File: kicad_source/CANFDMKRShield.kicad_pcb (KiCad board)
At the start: 2 copper layers, 60 x 23 mm, 13 parts, among them CN1 ARDUINO_MKR, CN2 CONN_01X04, SW1 SWITCH_SMALL, U1 MCP2517FD, U2 SN65HVD232, Y1 20MHz

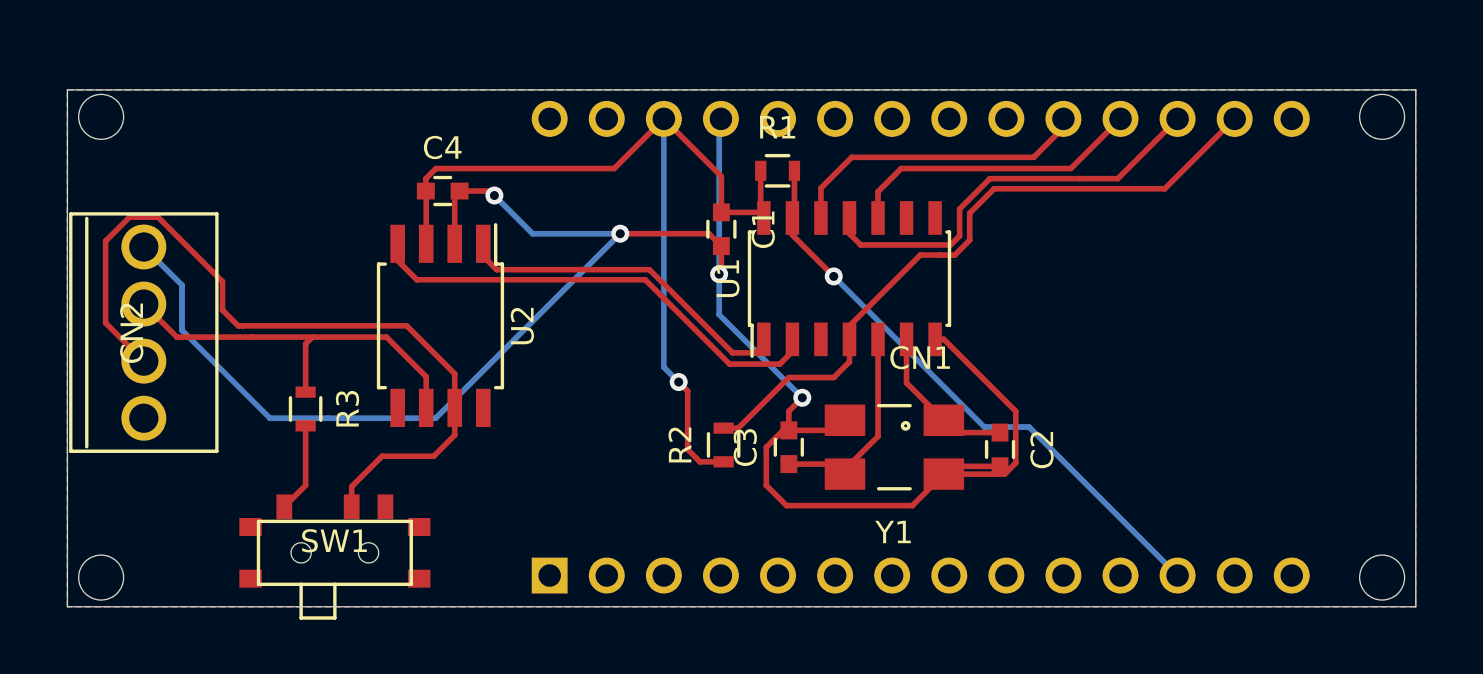
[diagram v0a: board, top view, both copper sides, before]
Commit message: added voltage regulators, updated images and pdf schematic
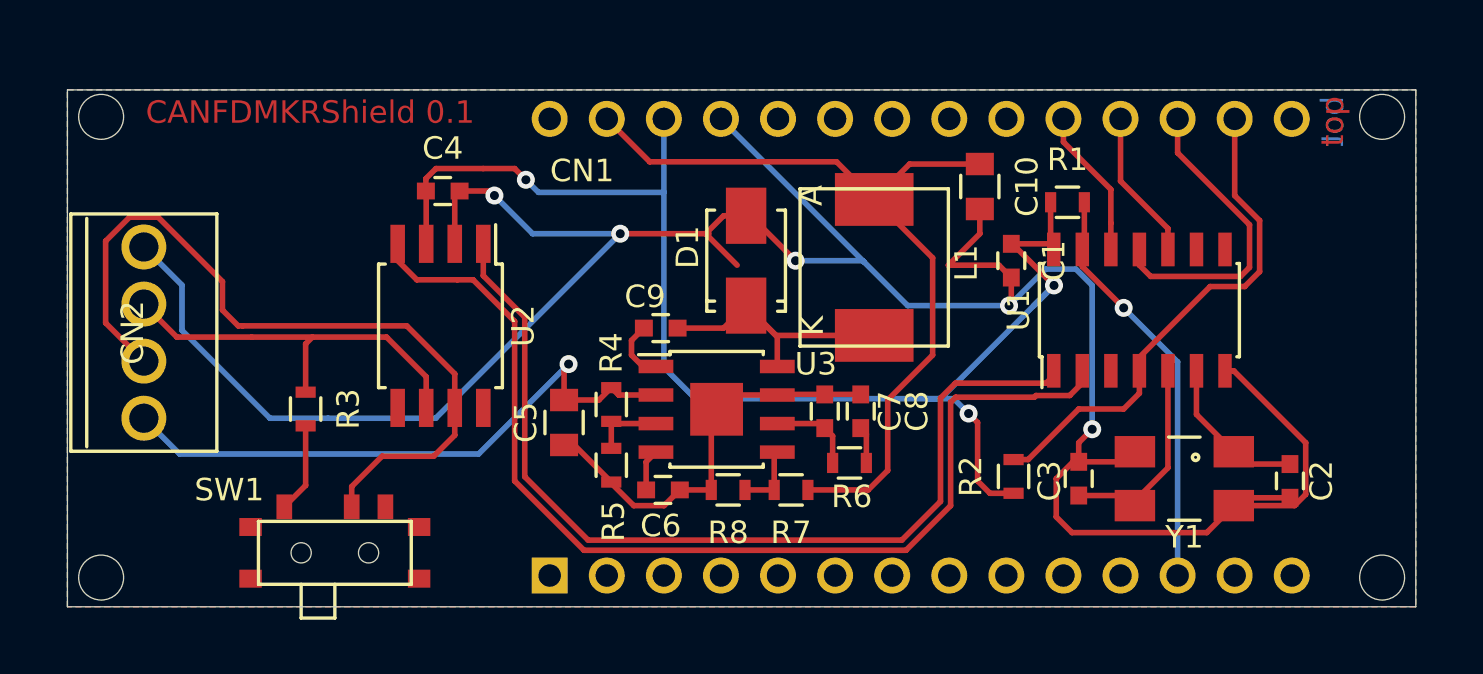
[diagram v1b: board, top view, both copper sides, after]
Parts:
- added C10: 10uF, capacitors:C_0805, F.Cu at (148.6, 93.3)
- added C5: 10uF, capacitors:C_0805, F.Cu at (130.1, 103.8)
- added C6: 4.7 nF, capacitors:C_0603, F.Cu at (134.5, 106.8)
- added C7: 110pF, capacitors:C_0603, F.Cu at (141.7, 103.3)
- added C8: 4.7 nF, capacitors:C_0603, F.Cu at (143.3, 103.3)
- added C9: 100nF, capacitors:C_0603, F.Cu at (134.4, 99.6)
- added D1: SSA34, diodes:SMA_Standard, F.Cu at (138.2, 96.6)
- added L1: 0624CDMCCDS-220MC, L_power:Sumida-0624CDMCCDS, F.Cu at (143.9, 96.9)
- added L2: Label, labels:generationmake_small_solder, F.Cu at (168.3, 100.2)
- added R4: DNI, resistors:R_0603, F.Cu at (132.2, 103.0)
- added R5: DNI, resistors:R_0603, F.Cu at (132.2, 105.7)
- added R6: 12k7, resistors:R_0603, F.Cu at (142.8, 105.6)
- added R7: 10k, resistors:R_0603, F.Cu at (140.2, 106.8)
- added R8: 1k9, resistors:R_0603, F.Cu at (137.4, 106.8)
- added U3: TPS54232, SOIC:SOIC-8-1EP_3.9x4.9mm_Pitch1.27mm, F.Cu at (136.9, 103.2)
- moved C1 13.0 mm to (150.0, 96.6)
- moved C2 13.0 mm to (162.4, 106.4)
- moved C3 13.0 mm to (153.0, 106.3)
- moved R1 13.0 mm to (152.5, 94.0)
- moved R2 13.0 mm to (150.1, 106.2)
- moved U1 13.0 mm to (155.7, 98.8)
- moved Y1 13.0 mm to (157.7, 106.3)
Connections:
- CN1 pad 27: (no net) -> +5V
- CN2 pad 4: (no net) -> VCC
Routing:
- net GND: track 88.8 -> 136.9 mm, vias 4 -> 5
- net +5V: track 0.00 -> 36.6 mm
- net VCC: track 0.00 -> 27.3 mm, vias 0 -> 1
- net /CAN_TX: track 15.2 -> 41.8 mm
- net /CAN_RX: track 21.0 -> 47.0 mm
- net +3V3: track 41.0 -> 60.5 mm, vias 1 -> 3
- net /PH: track 0.00 -> 13.0 mm
- net /MCP2517_CS: track 26.3 -> 18.4 mm
- net /MCP2517_INT: track 30.1 -> 22.6 mm
- net /MISO: track 13.6 -> 6.68 mm
- net /SCK: track 13.3 -> 6.68 mm
- net /MOSI: track 18.5 -> 13.9 mm
- net /COMP: track 0.00 -> 3.89 mm
- net /EN: track 0.00 -> 3.23 mm
- net /VSENSE: track 0.00 -> 3.04 mm
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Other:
- board text added: "CANFDMKRShield 0.1"
- board text added: "bot"
- board text added: "top"

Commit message: added dronecode CAN connectors, updated images and schematic pdf
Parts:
- added CN3: GH_SM04B-GHS-TB, Connector_JST:JST_GH_SM04B-GHS-TB_1x04-1MP_P1.25mm_Horizontal, F.Cu at (111.2, 96.0)
- added CN4: GH_SM04B-GHS-TB, Connector_JST:JST_GH_SM04B-GHS-TB_1x04-1MP_P1.25mm_Horizontal, F.Cu at (111.2, 104.9)
- moved CN2 11.7 mm to (120.4, 92.3), turned to 180 degrees
- moved R3 2.82 mm to (117.8, 105.9), turned to 180 degrees
- moved C4 2.77 mm to (126.8, 95.3), turned to 270 degrees
- moved U2 2.30 mm to (124.7, 101.8)
- moved L2 2.19 mm to (166.8, 98.6)
- moved SW1 0.61 mm to (119.3, 109.5)
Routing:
- net +5V: track 36.6 -> 79.2 mm, vias 0 -> 2
- net /CANL: track 17.9 -> 48.4 mm
- net GND: track 136.9 -> 152.5 mm, vias 5 -> 8
- net /CANH: track 34.8 -> 49.3 mm, vias 0 -> 2
- net VCC: track 27.3 -> 24.3 mm
- net Net-(R3-Pad2): track 3.99 -> 1.55 mm
- net /CAN_RX: track 47.0 -> 45.2 mm
- net +3V3: track 60.5 -> 59.8 mm

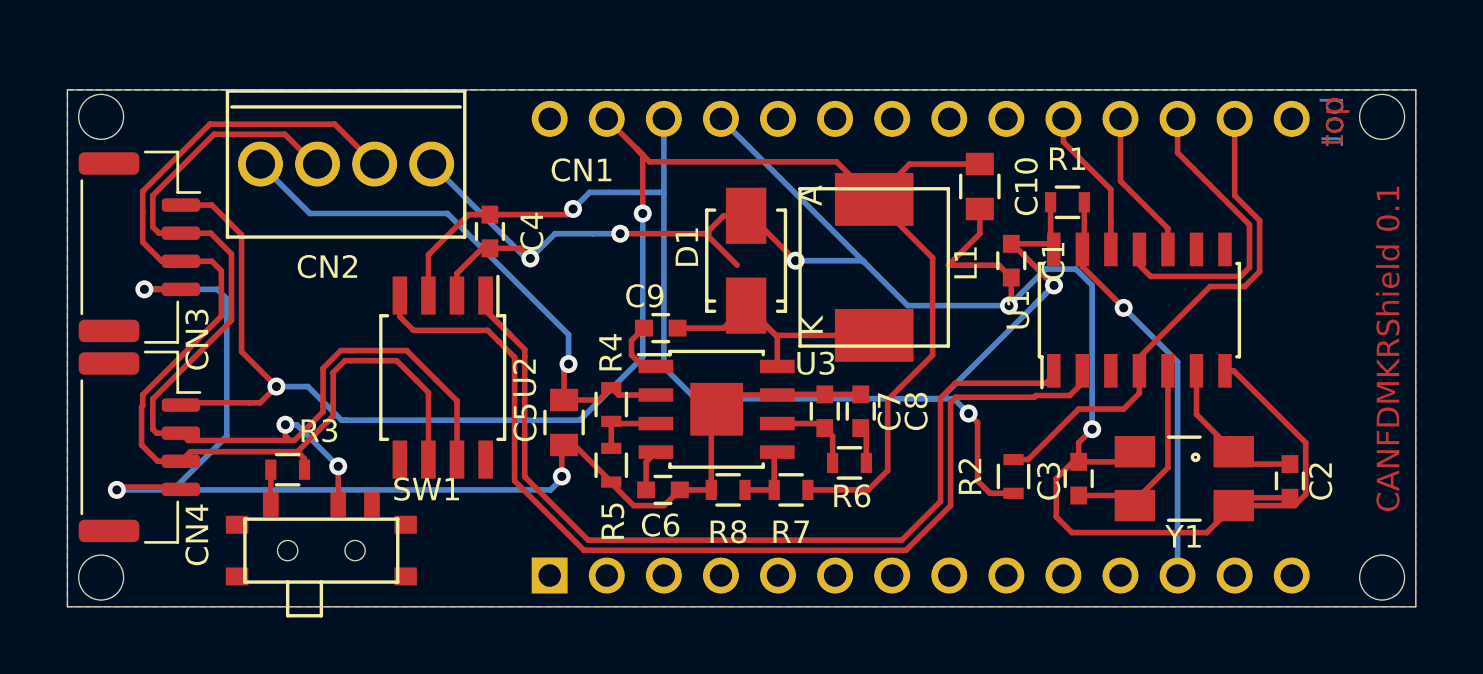
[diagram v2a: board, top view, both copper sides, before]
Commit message: updated board shape, changed switch type
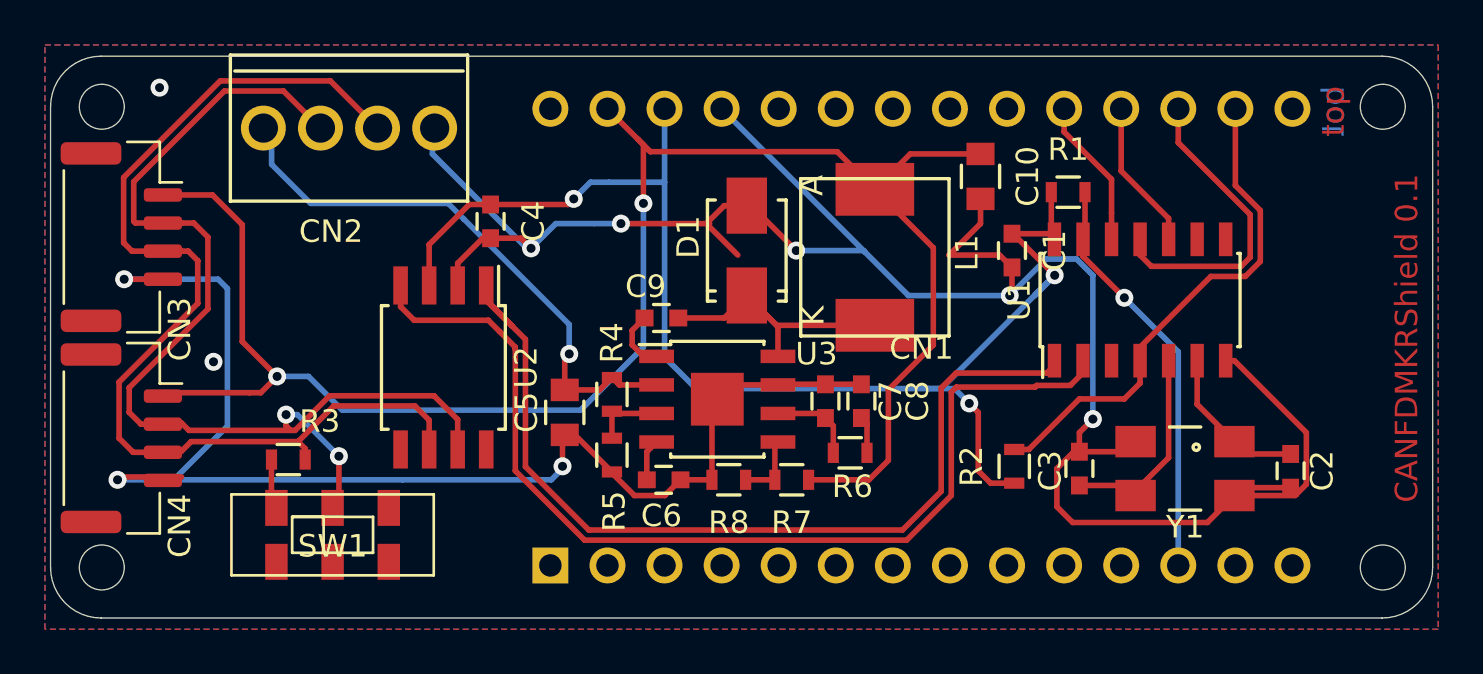
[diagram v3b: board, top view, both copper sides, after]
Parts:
- CN1: footprint MODULE_compute:ARDUINO_MKR_HOLES -> MODULE_compute:ARDUINO_MKR_HOLES_PINHEADER_EDGE
- SW1: value SWITCH_SMALL -> JS202011JCQN; footprint mechanical-switches:WE_450404015514 -> mechanical-switches:CK_JS202011JCQN
- moved CN2 1.61 mm to (120.5, 90.7)
- moved CN3 0.92 mm to (110.4, 95.5)
- moved CN4 0.89 mm to (110.4, 104.5)
- moved SW1 0.86 mm to (119.8, 108.8), turned to 0 degrees
- moved C10 0.45 mm to (148.6, 92.8)
- moved C2 0.45 mm to (162.4, 106.0)
- moved C3 0.45 mm to (153.0, 105.8)
- moved C4 0.45 mm to (126.8, 94.8)
- moved C5 0.45 mm to (130.1, 103.3)
- moved C6 0.45 mm to (134.5, 106.3)
- moved C7 0.45 mm to (141.7, 102.8)
- moved C8 0.45 mm to (143.3, 102.8)
- moved CN1 0.45 mm to (146.0, 100.0)
- moved L1 0.45 mm to (143.9, 96.5)
- moved R1 0.45 mm to (152.5, 93.5)
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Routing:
- net GND: track 152.5 -> 154.7 mm, vias 8 -> 10
- net VCC: track 24.3 -> 25.4 mm
- net /CANL: track 48.4 -> 47.4 mm
- net /CANH: track 49.3 -> 48.6 mm
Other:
- board size 60 x 23 mm -> 61.5 x 25 mm

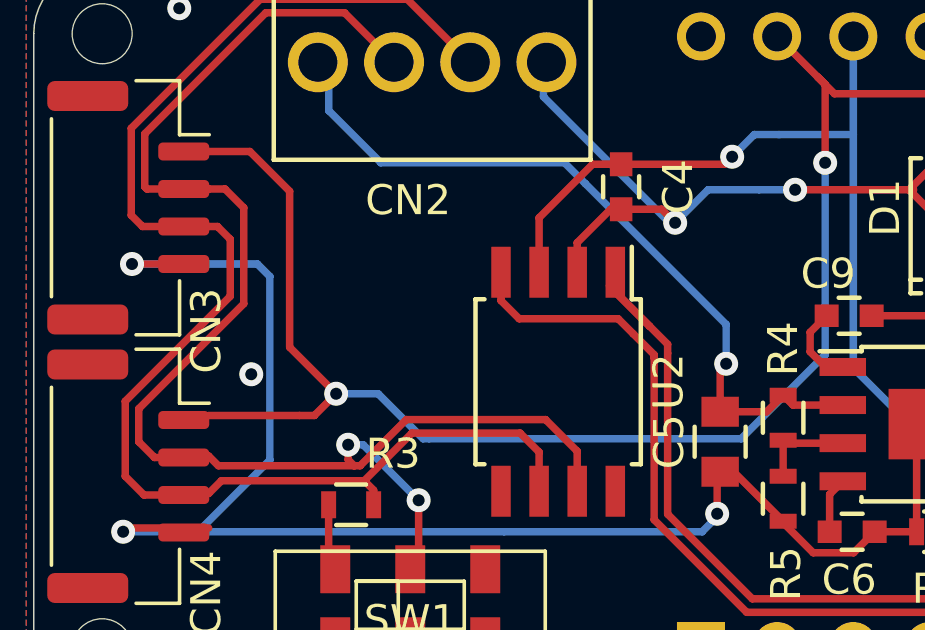
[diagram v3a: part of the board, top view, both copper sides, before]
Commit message: added diode D2 to connect CAN VCC to 5V
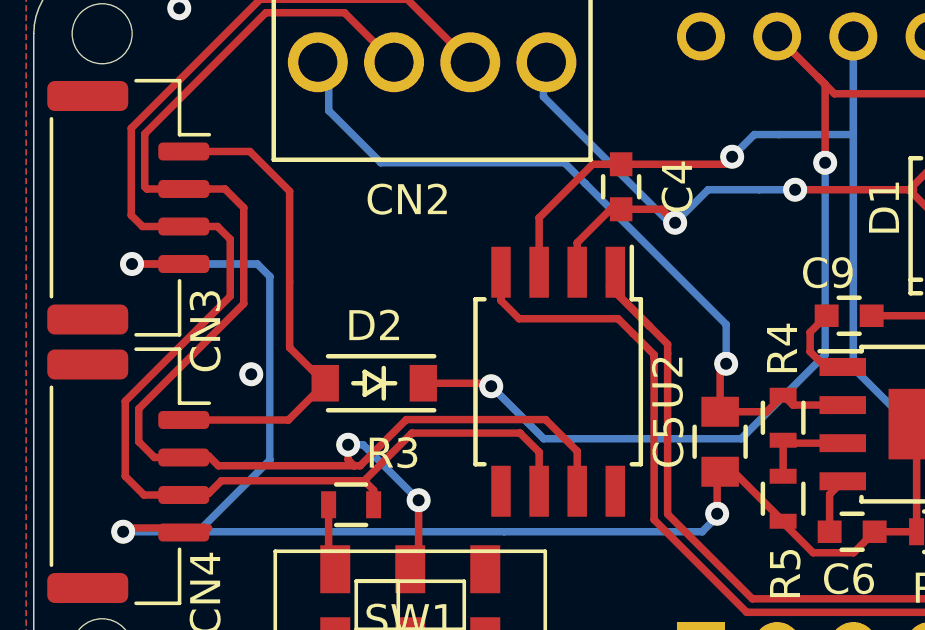
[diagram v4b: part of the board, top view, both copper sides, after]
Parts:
- added D2: DNI, diodes:SOD-123, F.Cu at (118.6, 101.4)
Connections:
- CN3 pad 1: +5V -> /CANVCC
- CN4 pad 1: +5V -> /CANVCC
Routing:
- net +5V: track 79.2 -> 61.3 mm
- net /CANVCC: track 0.00 -> 15.4 mm

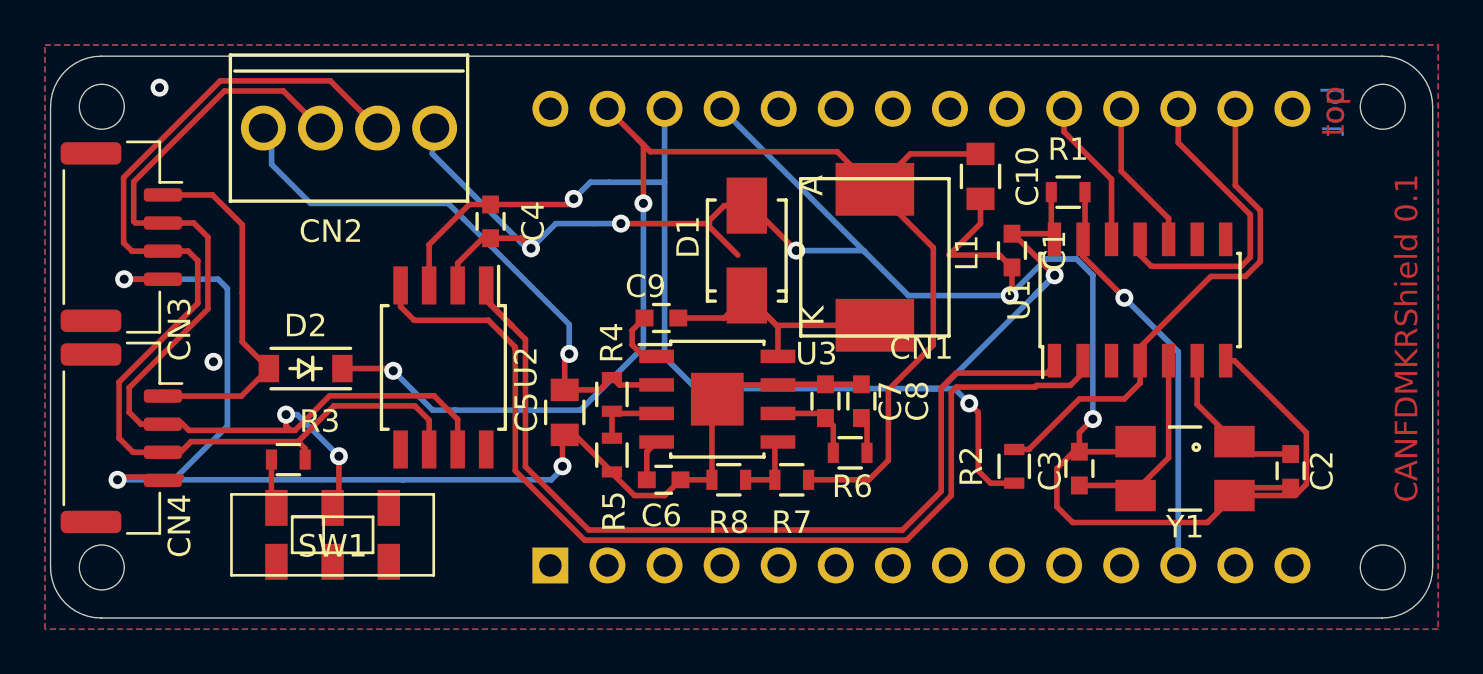
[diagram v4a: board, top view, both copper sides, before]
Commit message: added option to use different CS line for SPI
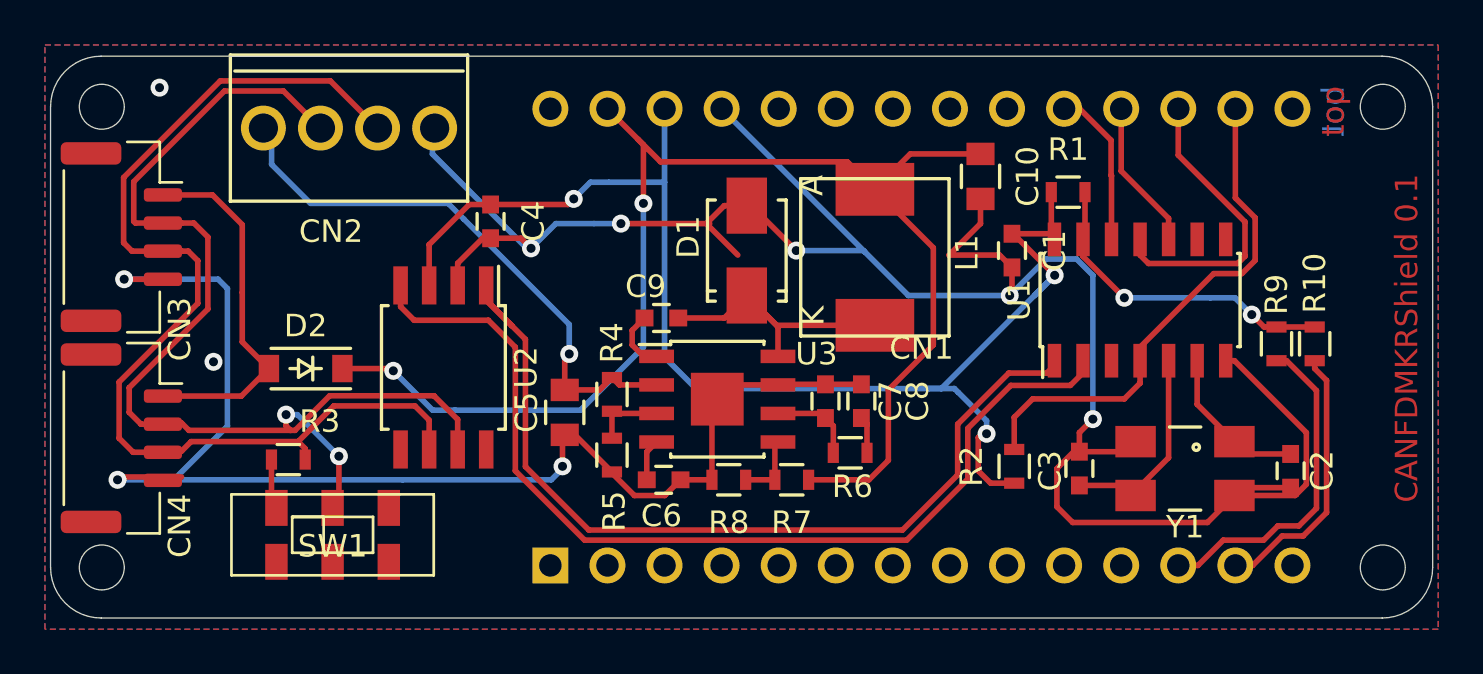
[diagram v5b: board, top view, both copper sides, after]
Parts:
- added R10: DNI, resistors:R_0603, F.Cu at (163.5, 100.3)
- added R9: 0R, resistors:R_0603, F.Cu at (161.8, 100.3)
- moved L2 1.29 mm to (168.1, 98.4)
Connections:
- CN1 pad 12: /MCP2517_CS -> /MCP2517_CS1
- CN1 pad 13: (no net) -> /MCP2517_CS2
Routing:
- net /MCP2517_CS1: track 0.00 -> 14.8 mm
- net /MCP2517_CS2: track 0.00 -> 12.0 mm
- net /MCP2517_CS: track 18.4 -> 14.5 mm, vias 1 -> 2
- net /CAN_RX: track 45.2 -> 43.8 mm
- net /CAN_TX: track 41.3 -> 40.0 mm

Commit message: defined type of crystal, updated 3d models of footprints
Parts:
- Y1: footprint crystals:Crystal_SMD_0603_4Pads -> crystals:Crystal_SMD_3.2x2.5mm_4Pad
- moved R2 16.1 mm to (162.0, 94.9)
- moved L2 3.00 mm to (168.1, 101.4)
- moved C2 2.23 mm to (160.2, 105.9)
- moved C3 1.07 mm to (154.1, 105.8)
- moved Y1 0.53 mm to (157.2, 105.8), turned to 0 degrees
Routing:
- net GND: track 154.7 -> 167.7 mm, vias 10 -> 13
- net /MCP2517_INT: track 23.1 -> 15.8 mm
- net /MCP2517_CS1: track 14.8 -> 12.6 mm
- net /OSC2: track 9.29 -> 8.13 mm
- net /OSC1: track 7.02 -> 5.87 mm
- net /MCP2517_CS2: track 12.0 -> 10.9 mm
- net /CAN_RX: track 43.8 -> 43.2 mm
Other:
- board text added: "Termination on<->off"
